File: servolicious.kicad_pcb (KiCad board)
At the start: 2 copper layers, 50.8 x 25.4 mm, 29 parts, among them J1 Conn_01x03_Pin, J10 Conn_01x03_Pin, J11 Conn_01x03_Pin, J12 Conn_01x03_Pin, J13 Conn_01x03_Pin, J14 Conn_01x03_Pin, J15 Conn_01x03_Pin, J16 Conn_01x03_Pin, J17 Barrel_Jack_MountingPin, J18 Conn_01x03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

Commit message: Update README for PCA9685 and rotate cap to allow it to be bent over
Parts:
- moved C1 2.78 mm to (108.2, 104.6), turned to -90 degrees
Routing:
- net +5V: track 151.8 -> 150.9 mm
- net Earth: vias 9 -> 18
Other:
- board text added: "Servolicious"
- board text added: "Stefan Buller 2025-07-03 V3.0"
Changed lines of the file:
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@@
 		)
 		(embedded_fonts no)
-		(model "${KICAD9_3DMODEL_DIR}/Connector_PinHeader_2.54mm.3dshapes/PinHeader_1x03_P2.54mm_Vertical.step"
+		(model "${KICAD9_3DMODEL_DIR}/Connector_PinHeader_2.54mm.3dshapes/PinHeader_1x03_P2.54mm_Vertical.wrl"
 			(offset
 				(xyz 0 0 0)
@@
 		)
 		(embedded_fonts no)
-		(model "${KICAD9_3DMODEL_DIR}/Connector_PinHeader_2.54mm.3dshapes/PinHeader_1x03_P2.54mm_Vertical.step"
+		(model "${KICAD9_3DMODEL_DIR}/Connector_PinHeader_2.54mm.3dshapes/PinHeader_1x03_P2.54mm_Vertical.wrl"
 			(offset
 				(xyz 0 0 0)
@@
 		)
 		(embedded_fonts no)
-		(model "${KICAD9_3DMODEL_DIR}/Connector_BarrelJack.3dshapes/BarrelJack_Horizontal.step"
+		(model "${KICAD9_3DMODEL_DIR}/Connector_BarrelJack.3dshapes/BarrelJack_Horizontal.wrl"
 			(offset
 				(xyz 0 0 0)
@@
 		)
 		(embedded_fonts no)
-		(model "${KICAD9_3DMODEL_DIR}/Connector_PinSocket_2.54mm.3dshapes/PinSocket_1x03_P2.54mm_Vertical.step"
+		(model "${KICAD9_3DMODEL_DIR}/Connector_PinSocket_2.54mm.3dshapes/PinSocket_1x03_P2.54mm_Vertical.wrl"
 			(offset
 				(xyz 0 0 0)
@@
 		)
 		(embedded_fonts no)
-		(model "${KICAD9_3DMODEL_DIR}/Capacitor_SMD.3dshapes/C_1206_3216Metric.step"
+		(model "${KICAD9_3DMODEL_DIR}/Capacitor_SMD.3dshapes/C_1206_3216Metric.wrl"
 			(offset
 				(xyz 0 0 0)
@@
 		)
 		(embedded_fonts no)
-		(model "${KICAD9_3DMODEL_DIR}/Connector_PinHeader_2.54mm.3dshapes/PinHeader_1x03_P2.54mm_Vertical.step"
+		(model "${KICAD9_3DMODEL_DIR}/Connector_PinHeader_2.54mm.3dshapes/PinHeader_1x03_P2.54mm_Vertical.wrl"
 			(offset
 				(xyz 0 0 0)
@@
 		)
 		(embedded_fonts no)
-		(model "${KICAD9_3DMODEL_DIR}/Connector_PinHeader_2.54mm.3dshapes/PinHeader_1x03_P2.54mm_Vertical.step"
+		(model "${KICAD9_3DMODEL_DIR}/Connector_PinHeader_2.54mm.3dshapes/PinHeader_1x03_P2.54mm_Vertical.wrl"
 			(offset
 				(xyz 0 0 0)
@@
 		)
 		(embedded_fonts no)
-		(model "${KICAD9_3DMODEL_DIR}/Capacitor_SMD.3dshapes/C_1206_3216Metric.step"
+		(model "${KICAD9_3DMODEL_DIR}/Capacitor_SMD.3dshapes/C_1206_3216Metric.wrl"
 			(offset
 				(xyz 0 0 0)
@@
 		)
 		(embedded_fonts no)
-		(model "${KICAD9_3DMODEL_DIR}/Connector_PinHeader_2.54mm.3dshapes/PinHeader_1x03_P2.54mm_Vertical.step"
+		(model "${KICAD9_3DMODEL_DIR}/Connector_PinHeader_2.54mm.3dshapes/PinHeader_1x03_P2.54mm_Vertical.wrl"
 			(offset
 				(xyz 0 0 0)
@@
 		)
 		(embedded_fonts no)
-		(model "${KICAD9_3DMODEL_DIR}/Package_SO.3dshapes/TSSOP-28_4.4x9.7mm_P0.65mm.step"
+		(model "${KICAD9_3DMODEL_DIR}/Package_SO.3dshapes/TSSOP-28_4.4x9.7mm_P0.65mm.wrl"
 			(offset
 				(xyz 0 0 0)
@@
 	(footprint "Capacitor_THT:C_Radial_D8.0mm_H11.5mm_P3.50mm"
 		(layer "F.Cu")
-		(at 110.335 106.426 180)
+		(at 108.204 104.648 -90)
 		(descr "C, Radial series, Radial, pin pitch=3.50mm, diameter=8mm, height=11.5mm, Non-Polar Electrolytic Capacitor")
 		(tags "C Radial series Radial pin pitch 3.50mm diameter 8mm height 11.5mm Non-Polar Electrolytic Capacitor")
 		(property "Reference" "C1"
-			(at 1.75 1.905 0)
+			(at 1.75 1.905 90)
 			(layer "F.SilkS")
 			(effects
@@
 		)
 		(property "Value" "C_Small_US"
-			(at 1.75 5.25 0)
+			(at 1.75 5.25 90)
 			(layer "F.Fab")
 			(effects
@@
 		)
 		(property "Datasheet" ""
-			(at 0 0 0)
+			(at 0 0 90)
 			(layer "F.Fab")
 			(hide yes)
@@
 		)
 		(property "Description" "capacitor, small US symbol"
-			(at 0 0 0)
+			(at 0 0 90)
 			(layer "F.Fab")
 			(hide yes)
@@
 		)
 		(fp_text user "${REFERENCE}"
-			(at 1.75 0 0)
+			(at 1.75 0 90)
 			(layer "F.Fab")
 			(effects
@@
 		)
 		(pad "1" thru_hole circle
-			(at 0 0 180)
+			(at 0 0 270)
 			(size 1.6 1.6)
 			(drill 0.8)
@@
 		)
 		(pad "2" thru_hole circle
-			(at 3.5 0 180)
+			(at 3.5 0 270)
 			(size 1.6 1.6)
 			(drill 0.8)
@@
 		)
 		(embedded_fonts no)
-		(model "${KICAD9_3DMODEL_DIR}/Connector_PinHeader_2.54mm.3dshapes/PinHeader_1x03_P2.54mm_Vertical.step"
+		(model "${KICAD9_3DMODEL_DIR}/Connector_PinHeader_2.54mm.3dshapes/PinHeader_1x03_P2.54mm_Vertical.wrl"
 			(offset
 				(xyz 0 0 0)
@@
 		)
 		(embedded_fonts no)
-		(model "${KICAD9_3DMODEL_DIR}/Connector_PinHeader_2.54mm.3dshapes/PinHeader_1x03_P2.54mm_Vertical.step"
+		(model "${KICAD9_3DMODEL_DIR}/Connector_PinHeader_2.54mm.3dshapes/PinHeader_1x03_P2.54mm_Vertical.wrl"
 			(offset
 				(xyz 0 0 0)
@@
 		)
 		(embedded_fonts no)
-		(model "${KICAD9_3DMODEL_DIR}/Connector_PinHeader_2.54mm.3dshapes/PinHeader_1x03_P2.54mm_Vertical.step"
+		(model "${KICAD9_3DMODEL_DIR}/Connector_PinHeader_2.54mm.3dshapes/PinHeader_1x03_P2.54mm_Vertical.wrl"
 			(offset
 				(xyz 0 0 0)
@@
 		)
 	)
+	(gr_text "Servolicious"
+		(at 93.472 104.394 0)
+		(layer "F.SilkS")
+		(effects
+			(font
+				(size 1 1)
+				(thickness 0.1)
+			)
+			(justify left bottom)
+		)
+	)
 	(gr_text "G"
 		(at 88.408 99.98 0)
@@
 		)
 	)
+	(gr_text "Stefan Buller\n2025-07-03\nV3.0"
+		(at 93.472 109.982 0)
+		(layer "F.SilkS")
+		(effects
+			(font
+				(size 1 1)
+				(thickness 0.1)
+			)
+			(justify left bottom)
+		)
+	)
 	(gr_text "G"
 		(at 101.108 99.98 0)
@@
 	)
 	(segment
-		(start 110.335 106.68)
-		(end 110.335 106.426)
-		(width 1)
+		(start 101.6 111.73)
+		(end 101.57 111.73)
+		(width 0.2)
 		(layer "F.Cu")
 		(net 1)
 	)
 	(segment
-		(start 101.6 111.73)
-		(end 101.57 111.73)
-		(width 0.2)
+		(start 112.5605 109.0045)
+		(end 108.204 104.648)
+		(width 1)
 		(layer "F.Cu")
 		(net 1)
@@
 	)
 	(segment
+		(start 112.5605 114.554)
+		(end 112.5605 109.0045)
+		(width 1)
+		(layer "F.Cu")
+		(net 1)
+	)
+	(segment
 		(start 104.14 111.73)
 		(end 104.11 111.73)
@@
 	)
 	(segment
-		(start 112.5605 114.554)
-		(end 112.5605 108.9055)
-		(width 1)
-		(layer "F.Cu")
-		(net 1)
-	)
-	(segment
 		(start 75.8015 112.7935)
 		(end 79.047 116.039)
@@
 	)
 	(segment
-		(start 112.5605 108.9055)
-		(end 110.335 106.68)
-		(width 1)
-		(layer "F.Cu")
-		(net 1)
-	)
-	(segment
 		(start 99.06 111.73)
 		(end 99.03 111.73)
@@
 	)
 	(segment
-		(start 107.696 102.616)
-		(end 110.335 105.255)
-		(width 1)
-		(layer "B.Cu")
-		(net 1)
-	)
-	(segment
 		(start 101.6 96.52)
 		(end 111.76 96.52)
@@
 	)
 	(segment
-		(start 110.335 105.255)
-		(end 110.335 106.426)
-		(width 1)
-		(layer "B.Cu")
-		(net 1)
-	)
-	(segment
-		(start 101.6 96.52)
-		(end 101.6 99.622)
-		(width 1)
-		(layer "B.Cu")
-		(net 1)
-	)
-	(segment
 		(start 104.594 102.616)
-		(end 107.696 102.616)
+		(end 106.172 102.616)
 		(width 1)
 		(layer "B.Cu")
@@
 	)
 	(segment
+		(start 101.6 96.52)
+		(end 101.6 99.622)
+		(width 1)
+		(layer "B.Cu")
+		(net 1)
+	)
+	(segment
 		(start 103.505 111.125)
 		(end 100.965 111.125)
@@
 	)
 	(segment
+		(start 106.172 102.616)
+		(end 108.204 104.648)
+		(width 1)
+		(layer "B.Cu")
+		(net 1)
+	)
+	(segment
 		(start 91.7625 108.163)
 		(end 102.419 108.163)
@@
 	)
 	(via
+		(at 66.04 102.87)
+		(size 0.6)
+		(drill 0.3)
+		(layers "F.Cu" "B.Cu")
+		(free yes)
+		(net 3)
+	)
+	(via
 		(at 108.458 112.014)
 		(size 0.6)
@@
 	)
 	(via
+		(at 97.79 115.062)
+		(size 0.6)
+		(drill 0.3)
+		(layers "F.Cu" "B.Cu")
+		(free yes)
+		(net 3)
+	)
+	(via
+		(at 105.41 104.14)
+		(size 0.6)
+		(drill 0.3)
+		(layers "F.Cu" "B.Cu")
+		(free yes)
+		(net 3)
+	)
+	(via
+		(at 76.2 102.87)
+		(size 0.6)
+		(drill 0.3)
+		(layers "F.Cu" "B.Cu")
+		(free yes)
+		(net 3)
+	)
+	(via
 		(at 88.9 101.6)
 		(size 0.6)
 		(drill 0.3)
+		(layers "F.Cu" "B.Cu")
+		(free yes)
+		(net 3)
+	)
+	(via
+		(at 88.9 95.25)
+		(size 0.6)
+		(drill 0.3)
+		(layers "F.Cu" "B.Cu")
+		(free yes)
+		(net 3)
+	)
+	(via
+		(at 88.9 97.79)
+		(size 0.6)
+		(drill 0.3)
+		(layers "F.Cu" "B.Cu")
+		(free yes)
+		(net 3)
+	)
+	(via
+		(at 101.6 95.25)
+		(size 0.6)
+		(drill 0.3)
+		(layers "F.Cu" "B.Cu")
+		(free yes)
+		(net 3)
+	)
+	(via
+		(at 76.2 95.25)
+		(size 0.6)
+		(drill 0.3)
+		(layers "F.Cu" "B.Cu")
+		(free yes)
+		(net 3)
+	)
+	(via
+		(at 76.2 97.79)
+		(size 0.6)
+		(drill 0.3)

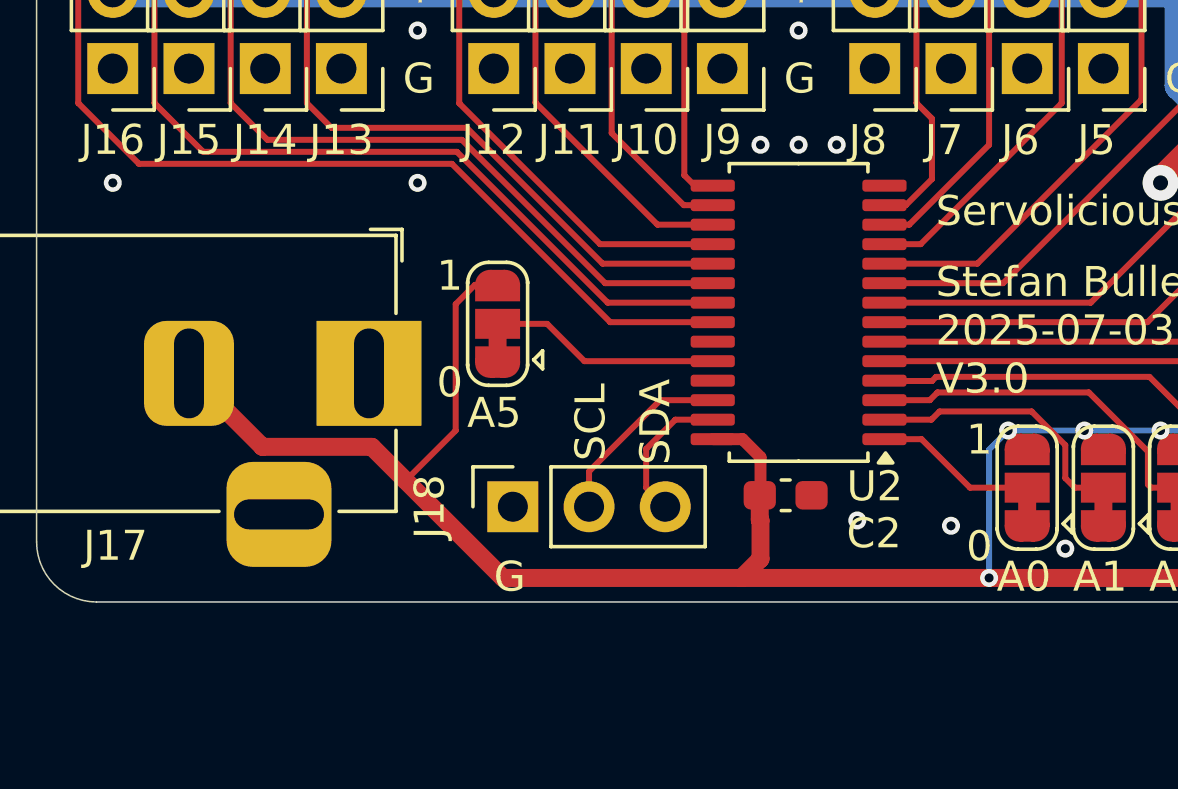
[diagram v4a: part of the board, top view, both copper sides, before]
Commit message: Interactive PWM control for finer grained management of servos
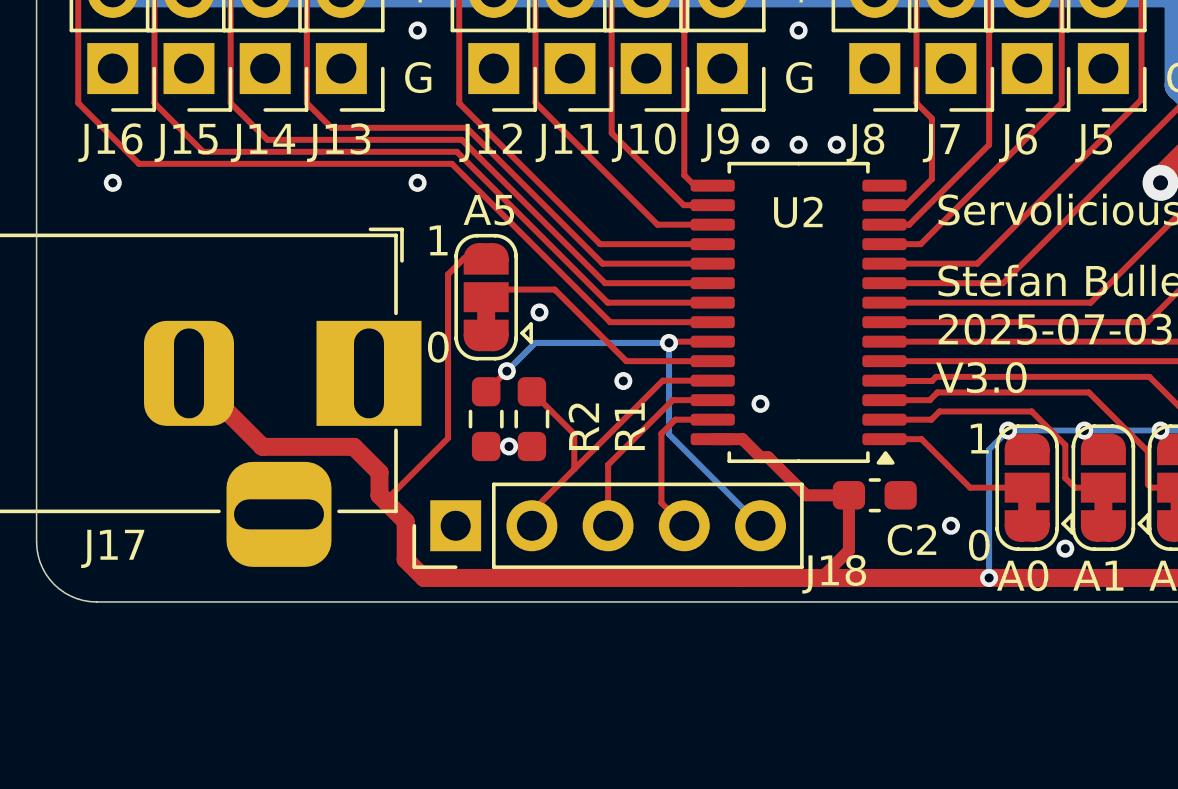
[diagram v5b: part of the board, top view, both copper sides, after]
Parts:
- added R1: R_Small, Resistor_SMD:R_0603_1608Metric_Pad0.98x0.95mm_HandSolder, F.Cu at (80.0, 110.7)
- added R2: R_Small, Resistor_SMD:R_0603_1608Metric_Pad0.98x0.95mm_HandSolder, F.Cu at (78.5, 110.7)
- J18: value Conn_01x03 -> Conn_01x05; footprint Connector_PinSocket_2.54mm:PinSocket_1x03_P2.54mm_Vertical -> Connector_PinHeader_2.54mm:PinHeader_1x05_P2.54mm_Vertical
- moved C2 2.97 mm to (91.4, 113.3)
- moved J18 2.01 mm to (77.5, 114.3)
- moved JP6 0.97 mm to (78.5, 106.7)
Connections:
- J18 pad 2: /SCL -> /CLK
- J18 pad 3: /SDA -> /SCL
- U2 pad 23: Earth -> /OE
- U2 pad 25: unconnected-(U2-EXTCLK-Pad25) -> /CLK
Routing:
- net /OE: track 0.00 -> 15.6 mm, vias 0 -> 2
- net /CLK: track 0.00 -> 11.5 mm
- net +5V: track 150.9 -> 156.2 mm
- net Earth: track 5.13 -> 6.65 mm, vias 18 -> 21
- net /A5: track 7.69 -> 8.65 mm
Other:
- board text removed: "SCL"
- board text removed: "SDA"
